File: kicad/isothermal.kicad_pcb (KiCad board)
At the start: 2 copper layers, 83.8 x 33 mm, 33 parts, among them IC80 ATTINY85, P60 CONN_2X1, P70 CONN_4X1, Q20 IRF610, U1 LM358, U30 78L05

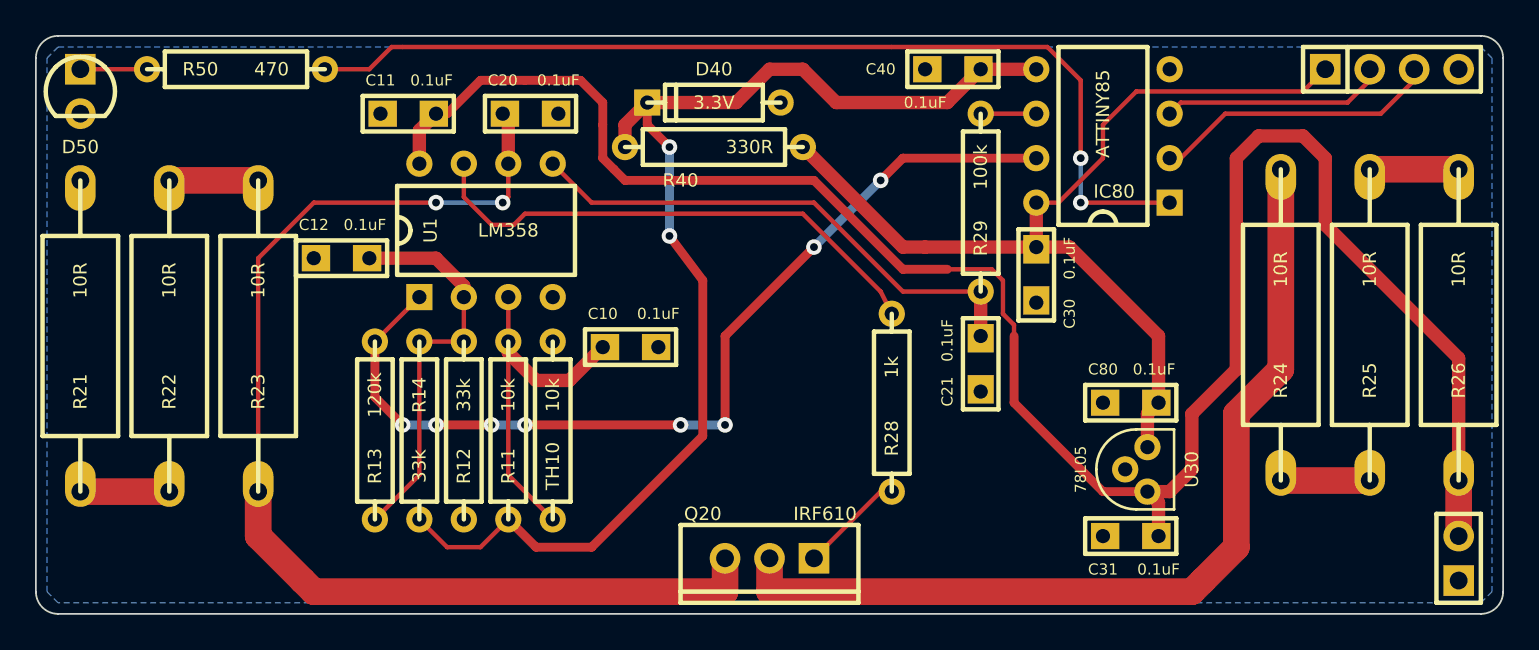
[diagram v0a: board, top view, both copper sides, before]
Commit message: used wider holes for the input protection diode.
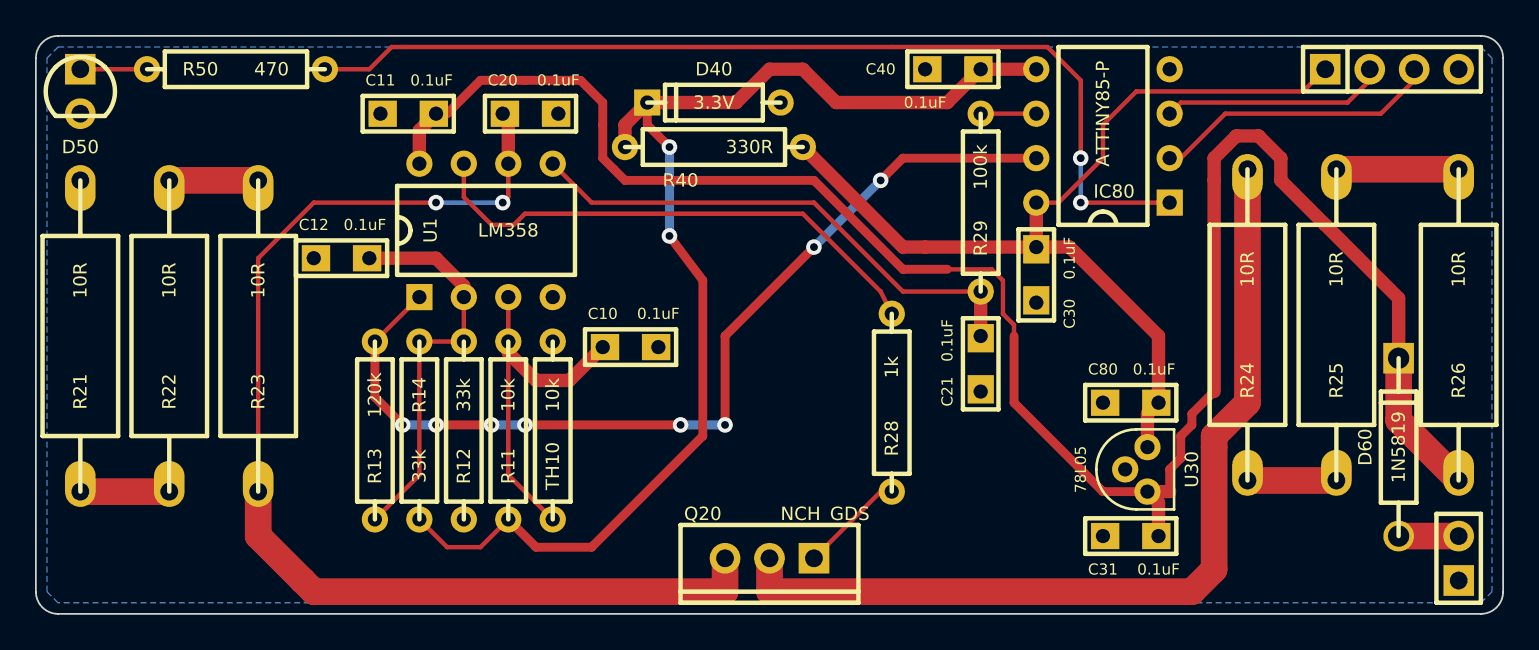
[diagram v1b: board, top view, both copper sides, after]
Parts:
- added D60: 1N5819, DIODE_1A_069A_04_PL, F.Cu at (193.4, 185.4)
- IC80: value ATTINY85 -> ATTINY85-P
- Q20: value IRF610 -> NCH_GDS
- moved G*** 4.44 mm to (184.8, 191.8)
- moved R24 1.91 mm to (184.8, 169.5)
- moved R25 1.91 mm to (189.9, 187.3)
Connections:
- P60 pad 2: 12V -> N-000001
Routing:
- net 12V: track 115.6 -> 111.7 mm
- net N-000001: track 0.00 -> 3.43 mm
- net N-000006: track 5.08 -> 6.98 mm
- net N-000008: track 52.3 -> 51.5 mm
